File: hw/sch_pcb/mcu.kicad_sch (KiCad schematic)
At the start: 54 parts, among them IC1 MAX14502AETL+, IC2 TMUX1574DYYR, J22 HEADER_2x03, J9 SD_Card-FPS009-4200-0, Q4 BC817-25, SW3 SW_Push, SW4 MCU_RST, U10 ATMEGA1284P-AU, U11 PCF85263A, U6 AT24CS64-SSHM, Y1 8 MHz, Y2 ABS07-120-32.768KHZ-T

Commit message: WIP, routing
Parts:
- BZ1: value Buzzer -> LET9032ES-03L-2.7-16-R; footprint (none) -> MLAB_BUZZER:MagneticBuzzer_LET9032ES-03L-2.7-16-R
- SW3: value SW_Push -> KMT031
- SW3: value SW_Push -> SKRTLAE010
- SW4: value MCU_RST -> KMT031
- renumbered IC2 to U12
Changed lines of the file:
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@@
       (effects (font (size 1 1)) (justify right))
     )
-    (property "Value" "MCU_RST" (at 259.08 156.21 90)
+    (property "Value" "KMT031" (at 259.08 156.21 90)
       (effects (font (size 1 1)) (justify right))
     )
@@
       (project "LION5CELL01"
         (path "/cca3030a-cb35-4155-89c2-3a41e5a0afad/80b69af2-66cc-4579-a230-ef2d06af8a00"
-          (reference "U10") (unit 1)
+          (reference "U11") (unit 1)
         )
       )
@@
       (effects (font (size 1.27 1.27)))
     )
-    (property "Value" "SW_Push" (at 194.31 153.67 0)
+    (property "Value" "KMT031" (at 194.31 153.67 0)
       (effects (font (size 1.27 1.27)))
     )
@@
       (project "LION5CELL01"
         (path "/cca3030a-cb35-4155-89c2-3a41e5a0afad/80b69af2-66cc-4579-a230-ef2d06af8a00"
-          (reference "IC1") (unit 1)
+          (reference "U10") (unit 1)
         )
       )
@@
       (project "LION5CELL01"
         (path "/cca3030a-cb35-4155-89c2-3a41e5a0afad/80b69af2-66cc-4579-a230-ef2d06af8a00"
-          (reference "U12") (unit 1)
+          (reference "U14") (unit 1)
         )
       )
@@
       (effects (font (size 1.27 1.27)) (justify left))
     )
-    (property "Value" "Buzzer" (at 69.85 81.28 0)
+    (property "Value" "LET9032ES-03L-2.7-16-R" (at 69.85 81.28 0)
       (effects (font (size 1.27 1.27)) (justify left))
     )
-    (property "Footprint" "" (at 79.375 77.47 90)
+    (property "Footprint" "MLAB_BUZZER:MagneticBuzzer_LET9032ES-03L-2.7-16-R" (at 79.375 77.47 90)
       (effects (font (size 1.27 1.27)) hide)
     )
@@
   (symbol (lib_id "MLAB_IO:TMUX1574DYYR") (at 242.57 110.49 0) (unit 1)
     (in_bom yes) (on_board yes) (dnp no) (fields_autoplaced)
-    (property "Reference" "IC2" (at 255.27 102.87 0)
+    (property "Reference" "U12" (at 255.27 102.87 0)
       (effects (font (size 1.27 1.27)))
     )
@@
       (project "LION5CELL01"
         (path "/cca3030a-cb35-4155-89c2-3a41e5a0afad/80b69af2-66cc-4579-a230-ef2d06af8a00"
-          (reference "IC2") (unit 1)
+          (reference "U12") (unit 1)
         )
       )
@@
       (project "LION5CELL01"
         (path "/cca3030a-cb35-4155-89c2-3a41e5a0afad/80b69af2-66cc-4579-a230-ef2d06af8a00"
-          (reference "U11") (unit 1)
+          (reference "U13") (unit 1)
         )
       )
@@
       (effects (font (size 1.27 1.27)))
     )
-    (property "Value" "SW_Push" (at 194.31 139.7 0)
+    (property "Value" "SKRTLAE010" (at 194.31 139.7 0)
       (effects (font (size 1.27 1.27)))
     )

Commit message: WIP
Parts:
- C36: UST_ID 5c70984812875079b91f8bf2 -> (none)
- R17: UST_ID 5c70984512875079b91f8956 -> (none)
- R23: UST_ID 5c70984512875079b91f8962 -> (none)
- SW3: symbol Switch:SW_Push -> MLAB_SW:SW_Push_shield
- U10: UST_ID 5c70984412875079b91f888e -> (none)
- U11: UST_ID 5c70984612875079b91f8a0c -> (none)
- U6: UST_ID 5c70984712875079b91f8b99 -> (none)
- Y2: UST_ID 5c70984712875079b91f8b1b -> (none)
- renumbered R55 to R54, R56 to R55, R58 to R57, R59 to R58, R60 to R59
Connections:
- net GND: now also SW3.GND (SHIELD)
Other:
- moved on the sheet: R58, SW3

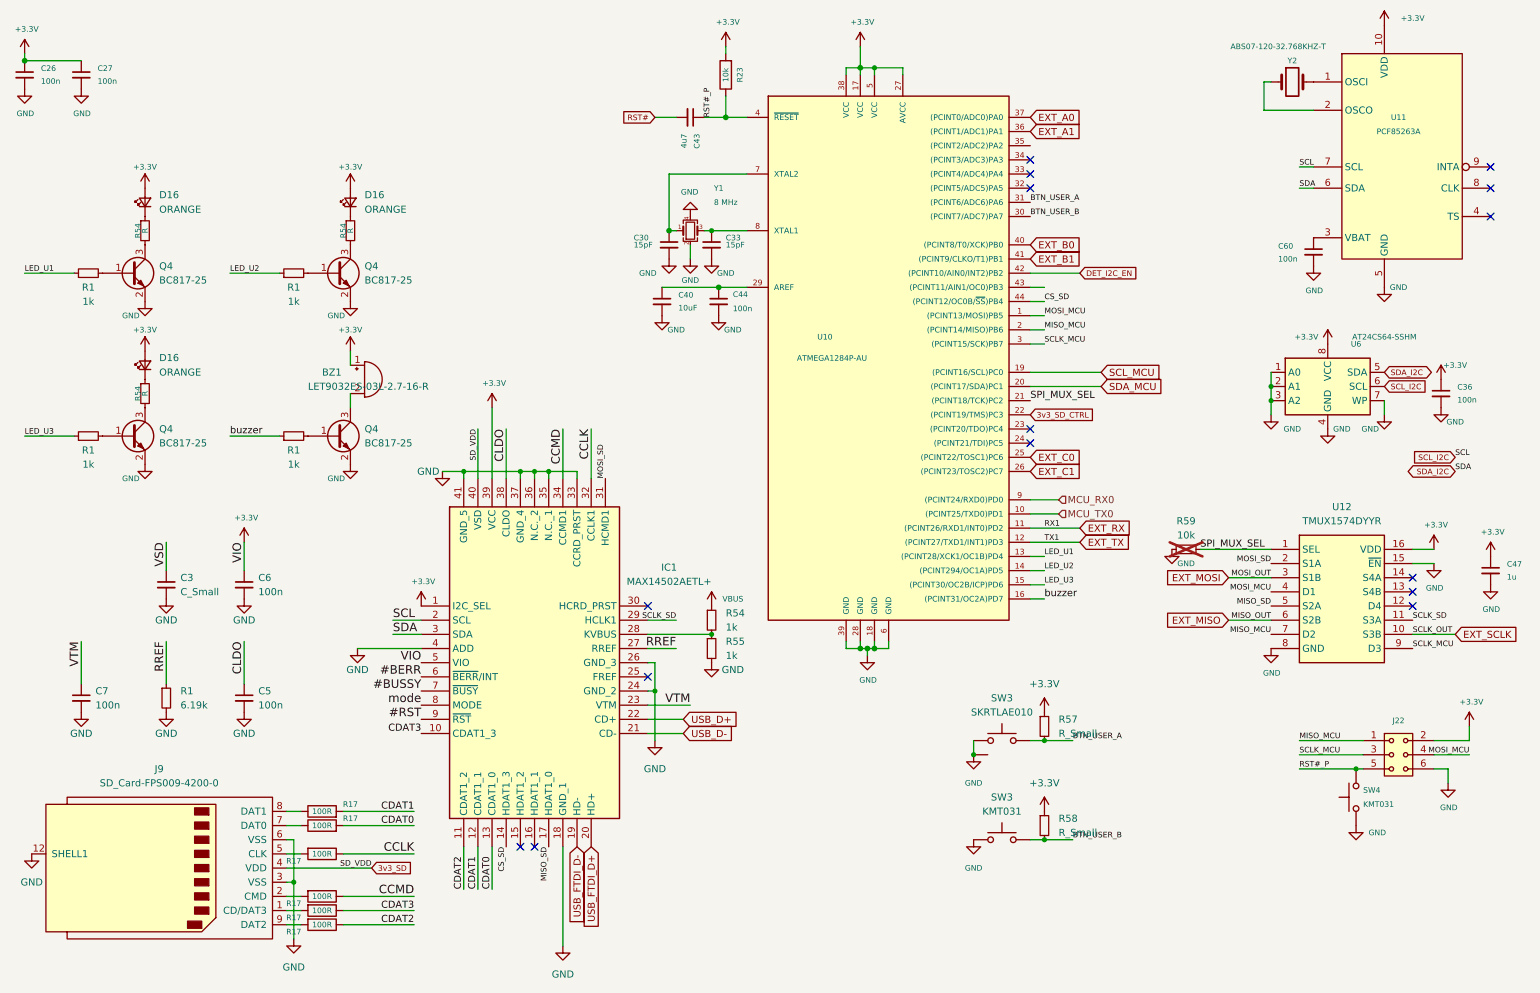
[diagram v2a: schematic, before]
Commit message: wip, split power adapter to BATDATSOCKET01
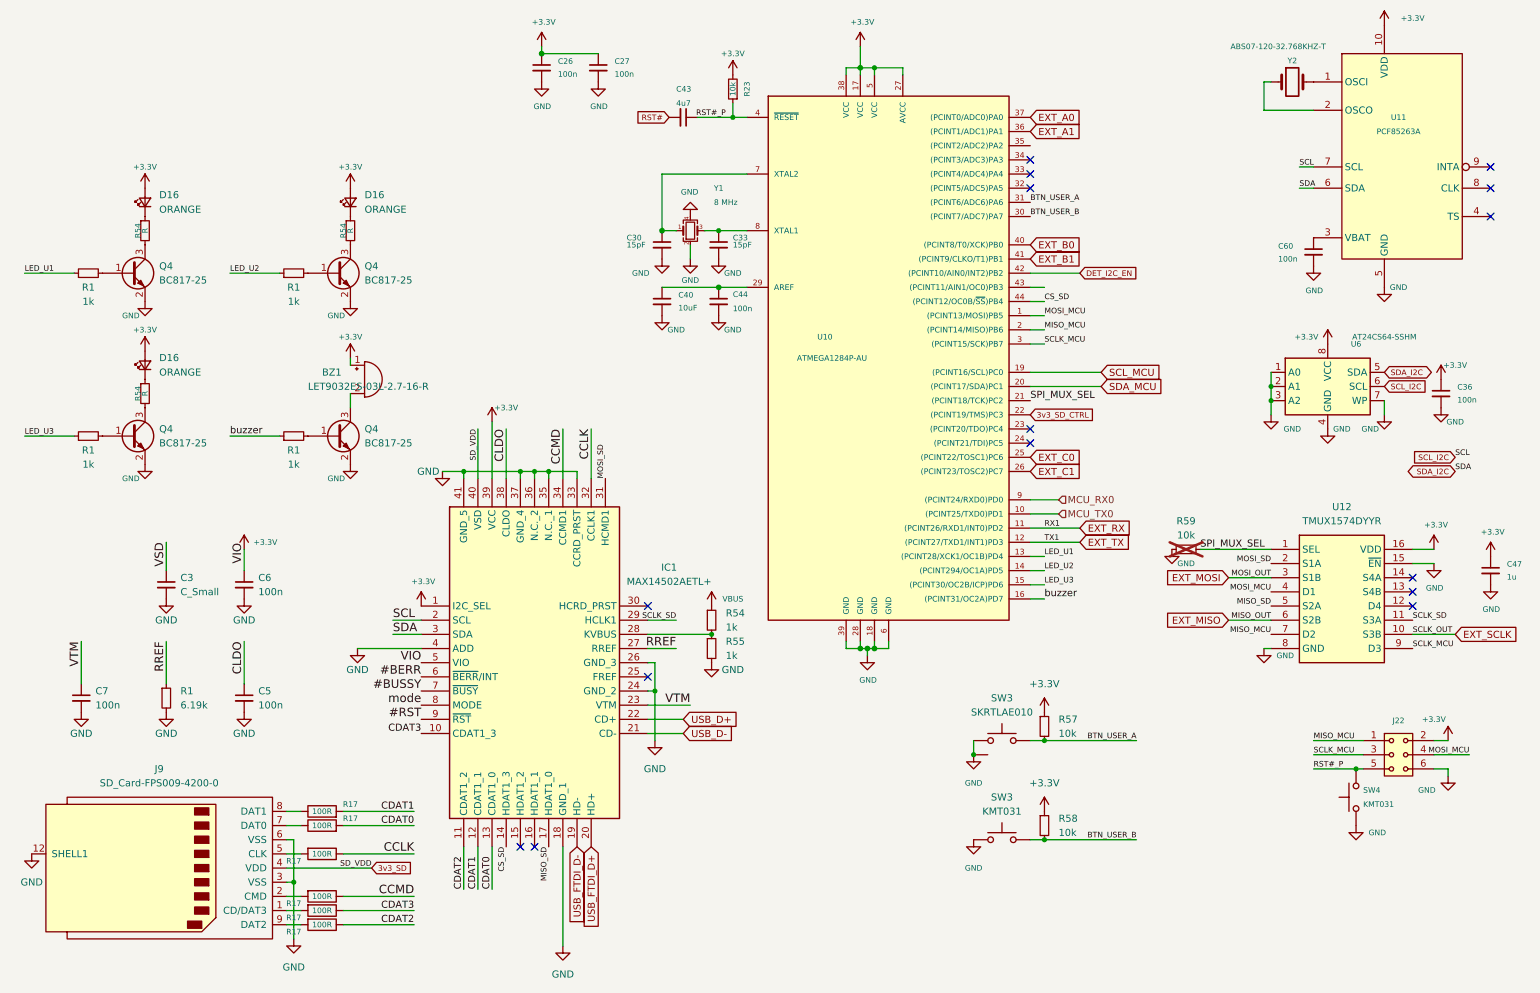
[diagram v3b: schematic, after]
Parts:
- R17: UST_ID (none) -> 5c70984512875079b91f8977
- R23: symbol SPACEDOS01A_PCB01A-rescue:R-device-DATALOGGER01A-rescue-CCP2019V01A-rescue -> Device:R_Small; UST_ID (none) -> 5c70984612875079b91f899f
- R57, R58: value R_Small -> 10k; UST_ID (none) -> 5c70984612875079b91f899f
- R59: UST_ID (none) -> 5c70984612875079b91f899f; now left out of the parts list
- SW3, SW4: UST_ID (none) -> 612515a61287500165a9771d
- U10: Height (none) -> 1.1; UST_ID (none) -> 5c70984412875079b91f888e
- U11: Height (none) -> 1.1; I2C (none) -> 0x; UST_ID (none) -> 5c70984612875079b91f8a0c
- U6: Height (none) -> 1.5; UST_ID (none) -> 5c70984712875079b91f8b99
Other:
- company: (none) -> MLAB.cz
- title: (none) -> BATDATUNTI01
- moved on the sheet: C26, C27, C30, C33, C43, R23

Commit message: WIP, add ust ID for existing parts
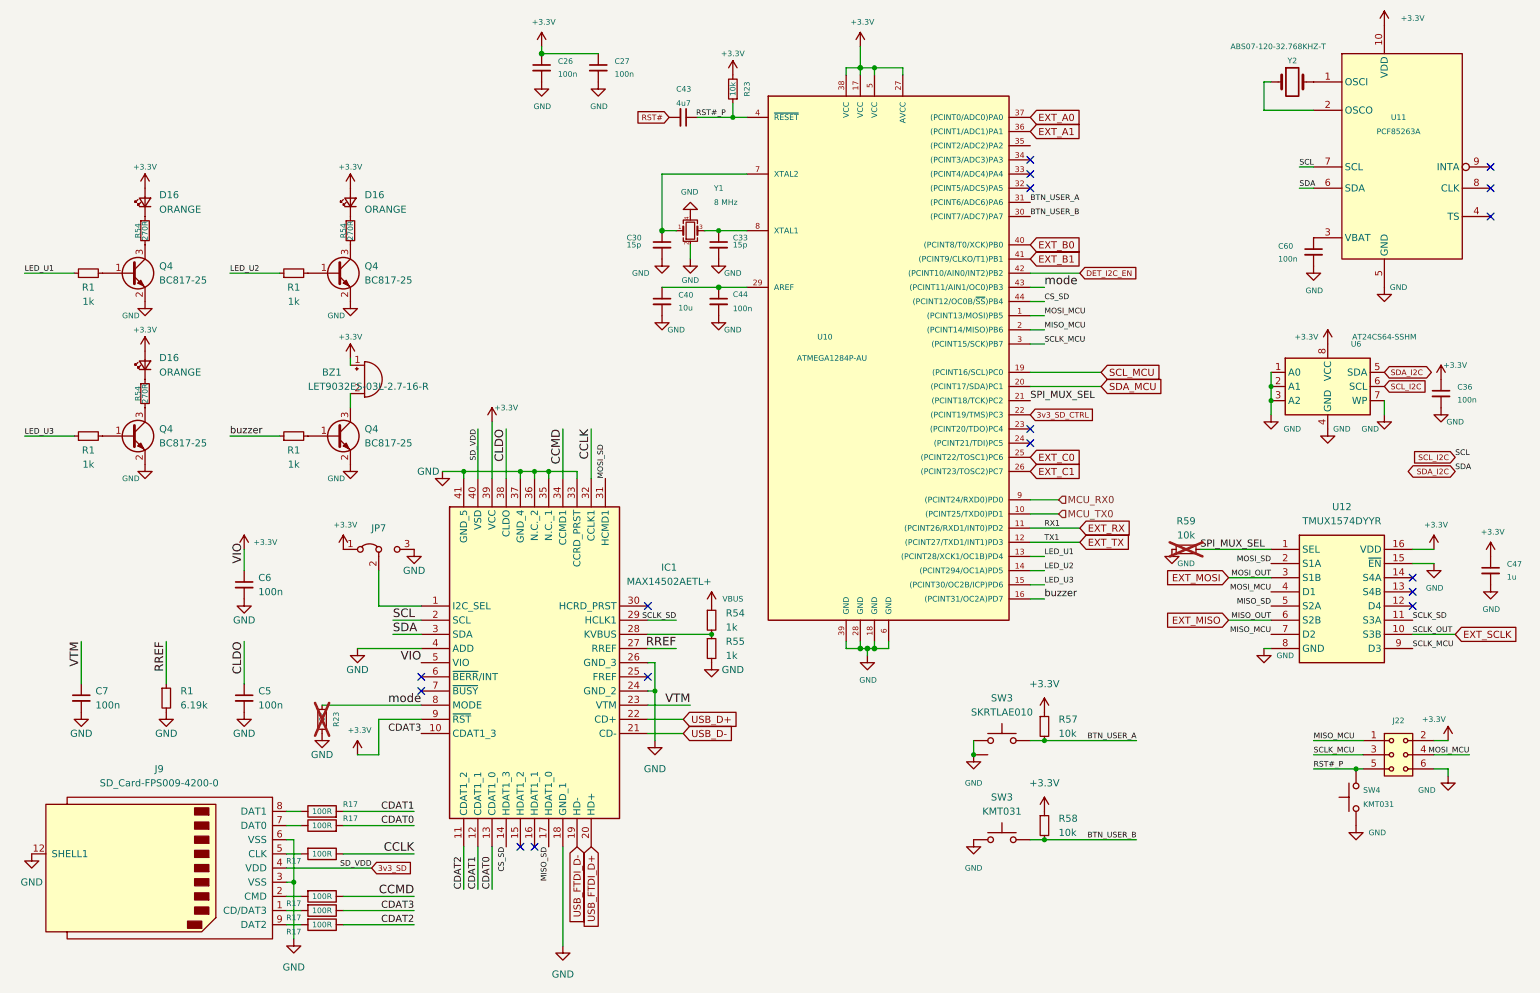
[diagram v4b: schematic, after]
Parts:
- removed C3: C_Small, Capacitor_SMD:C_0805_2012Metric, symbol Device:C_Small
- added JP7: Jumper_3_Bridged12, Jumper:SolderJumper-3_P1.3mm_Bridged2Bar12_RoundedPad1.0x1.5mm, symbol Jumper:Jumper_3_Bridged12
- added R23: 10k, Resistor_SMD:R_0805_2012Metric, symbol Device:R_Small
- BZ1: UST_ID (none) -> 5fa0f13812875025b3977890
- C26, C27, C36, C44, C5, C6, C60, C7: UST_ID (none) -> 5c70984712875079b91f8b4c
- C30, C33: value 15pF -> 15p; UST_ID (none) -> 5c70984712875079b91f8b32
- C40: value 10uF -> 10u; UST_ID (none) -> 5c70984712875079b91f8b53
- C43: UST_ID (none) -> 5c70984712875079b91f8b52
- C47: UST_ID (none) -> 5c70984712875079b91f8b50
- J22: UST_ID (none) -> x
- J9: UST_ID (none) -> 5cdd24d5128750448edda353
- Q4: UST_ID (none) -> 5c70984712875079b91f8aea
- R1, R54, R55: UST_ID (none) -> 5c70984512875079b91f898c
- R54: value R -> 270R
- Y2: UST_ID (none) -> 5c70984712875079b91f8b1b
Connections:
- net #RST is gone; now on net +3.3V: IC1.9 (~{RST})
- net +3.3V: now also JP7.1 (A); no longer IC1.1 (I2C_SEL)
- net GND: now also JP7.3 (B), R23.1
- net mode: now also U10.43 ((PCINT11/AIN1/OC0)PB3), R23.2
- net #BERR: no longer names the net of IC1.6 (~{BERR}/INT)
- net #BUSSY: no longer names the net of IC1.7 (~{BUSY})
- new net: IC1.1 (I2C_SEL), JP7.2 (C)
- no-connect marks 15 -> 17

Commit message: WIP, schematic improvements, bigger page, reststructualized
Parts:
- removed BZ1: LET9032ES-03L-2.7-16-R, MLAB_BUZZER:MagneticBuzzer_LET9032ES-03L-2.7-16-R, symbol Device:Buzzer
- removed C26, C27, C36, C44, C5, C6, C60, C7: 100n, Capacitor_SMD:C_0805_2012Metric, symbol Device:C_Small
- removed C30, C33: 15p, Capacitor_SMD:C_0805_2012Metric, symbol Device:C_Small
- removed C40: 10u, Capacitor_SMD:C_0805_2012Metric, symbol Device:C_Small
- removed C43: 4u7, Capacitor_SMD:C_0805_2012Metric, symbol Device:C_Small
- removed C47: 1u, Capacitor_SMD:C_0805_2012Metric, symbol Device:C_Small
- removed D16 (x3): ORANGE, Mlab_D:SMD_LED_RIGHT_KINGBRIGHT_1605, symbol Device:LED_Small
- removed IC1: MAX14502AETL+, Mlab_IO:QFN40P500X500X80-41N, symbol MLAB_IO:MAX14502AETL+
- removed J22: HEADER_2x03, Mlab_Pin_Headers:SMD_2x03, symbol MLAB_HEADER:HEADER_2x03
- removed J9: SD_Card-FPS009-4200-0, Mlab_CON:FPS009-4200-0, symbol MLAB_CONNECTORS:SD_Card-FPS009-4200-0
- removed JP7: Jumper_3_Bridged12, Jumper:SolderJumper-3_P1.3mm_Bridged2Bar12_RoundedPad1.0x1.5mm, symbol Jumper:Jumper_3_Bridged12
- removed Q4 (x4): BC817-25, Package_TO_SOT_SMD:SOT-23-3, symbol Device:Q_NPN_BEC
- removed R1 (x4), R54, R55: 1k, Resistor_SMD:R_0805_2012Metric, symbol Device:R_Small
- removed R1: 6.19k, Resistor_SMD:R_0805_2012Metric, symbol Device:R_Small
- removed R17 (x6): 100R, Resistor_SMD:R_0805_2012Metric, symbol SPACEDOS02A_PCB01A-rescue:R-device-DATALOGGER01A-rescue-CCP2019V01A-rescue-SPAC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
- removed R23 (x2), R57, R58, R59: 10k, Resistor_SMD:R_0805_2012Metric, symbol Device:R_Small
- removed R54 (x3): 270R, Resistor_SMD:R_0805_2012Metric, symbol Device:R_Small
- removed SW3, SW4: KMT031, Mlab_SW:KMT031 NGJ LHS C&K, symbol Switch:SW_Push
- removed SW3: SKRTLAE010, Mlab_SW:SKRT, symbol MLAB_SW:SW_Push_shield
- removed U10: ATMEGA1284P-AU, Package_QFP:TQFP-44_10x10mm_P0.8mm, symbol SPACEDOS01A_PCB01A-rescue:ATMEGA1284P-AU-atmel-DATALOGGER01A-rescue-CCP2019V01A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
- removed U11: PCF85263A, Package_SO:TSSOP-10_3x3mm_P0.5mm, symbol MLAB_IO:PCF85263A
- removed U12: TMUX1574DYYR, Mlab_IO:SOT-23-16 THIN, symbol MLAB_IO:TMUX1574DYYR
- removed U6: AT24CS64-SSHM, Package_SO:SOIC-8_3.9x4.9mm_P1.27mm, symbol Memory_EEPROM:AT24CS64-SSHM
- removed Y1: 8 MHz, Crystal:Crystal_SMD_3225-4Pin_3.2x2.5mm, symbol Device:Crystal_GND24_Small
- removed Y2: ABS07-120-32.768KHZ-T, Mlab_XTAL:ABS07, symbol SPACEDOS01A_PCB01A-rescue:Crystal-device-DATALOGGER01A-rescue-CCP2019V01A-rescue
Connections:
- no-connect marks 17 -> 0
